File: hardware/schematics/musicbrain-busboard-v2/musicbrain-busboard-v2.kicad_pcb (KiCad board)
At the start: 2 copper layers, 200 x 115 mm, 94 parts, among them J1 SLOT 1, J10 EXP, J11 DISPLAY, J12 QWIIC, J13 MIDI IN1, J14 MIDI IN2, J15 MIDI OUT, J16 CAN, J17 AUDIO/CODEC, J18 TUNE, J19 DLG1, J2 SLOT 2, J20 DLG2, J21 EXPANSION, J3 SLOT 3, J4 SLOT 4, J5 SLOT 5, J6 SLOT 6, J7 HUB 1, J8 HUB 2, J9 PWR IN, U1 Teensy 4.1, U10 H11L1, U11 74LVC1G17, U12 SN65HVD230, U13 74LVC1G17, U2 R-78E5.0-0.5, U3 AMS1117-3.3, U4 74HC154, U5 74HC165, U6 74HC165, U7 74LVC1G125, U8 74LVC245, U9 H11L1

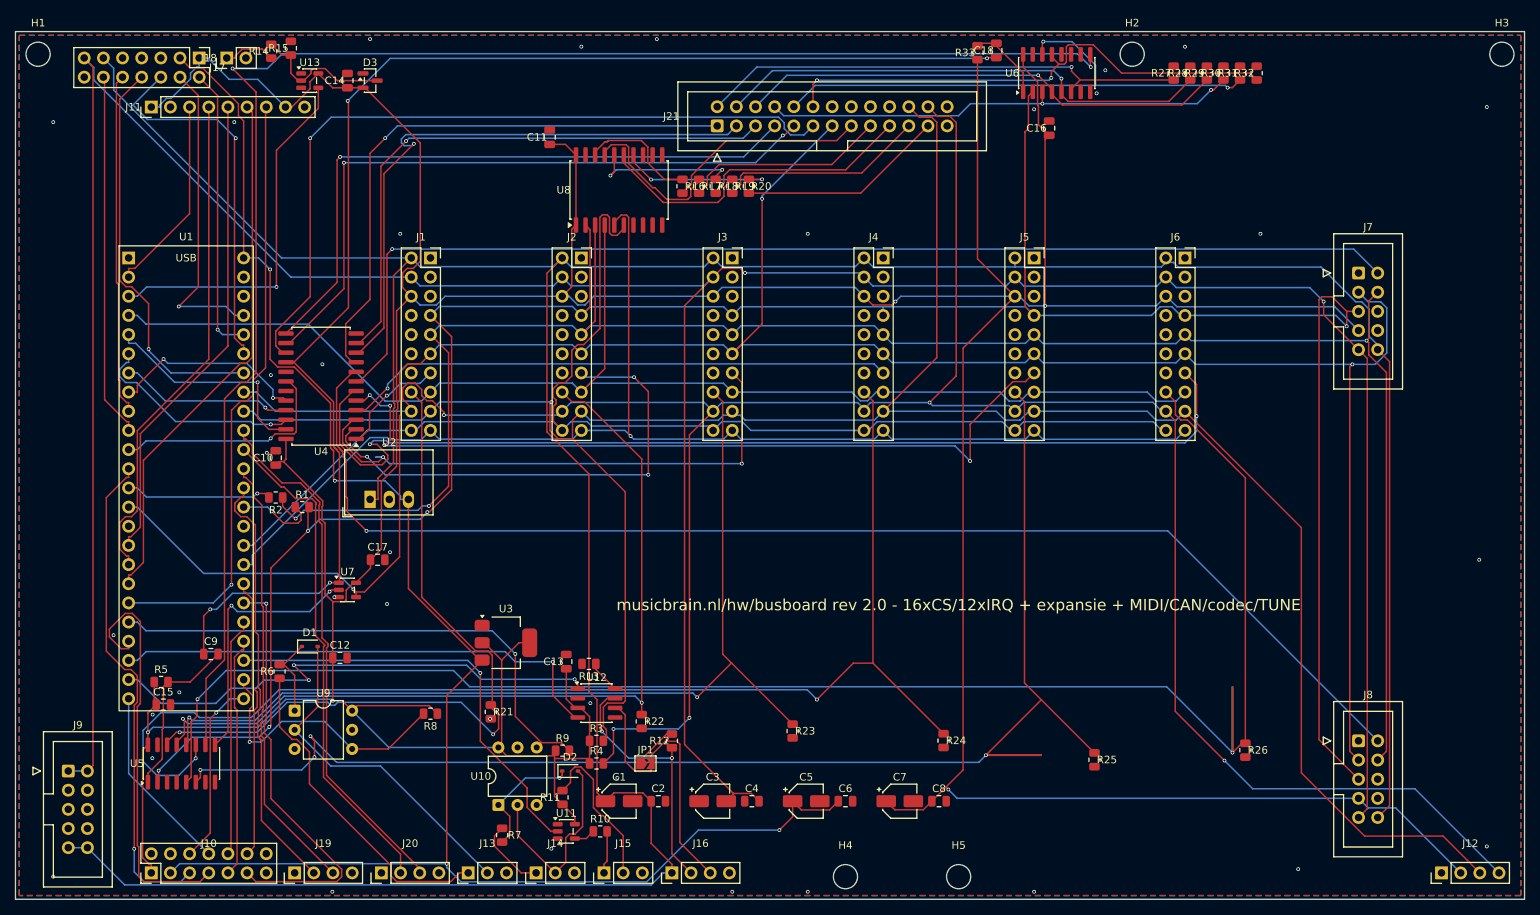
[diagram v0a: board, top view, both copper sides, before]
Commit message: busboard-v2: connector-labels verschoven (uit onder de headers)
Reference-labels van J7-J11/J17/J18/J21 handmatig verplaatst zodat ze niet meer
onder de connector-body vallen. KiCad heeft bij het opslaan het hele bestand
naar z'n native format herschreven (vandaar de grote diff); koper/connectiviteit
ongewijzigd - DRC 0 violations / 0 unconnected geverifieerd. Labelposities zijn
in gen_bus2_pcb.py REF_AT gesynct zodat een regeneratie ze behoudt.

Co-Authored-By: Claude Opus 4.8 <noreply@anthropic.com>
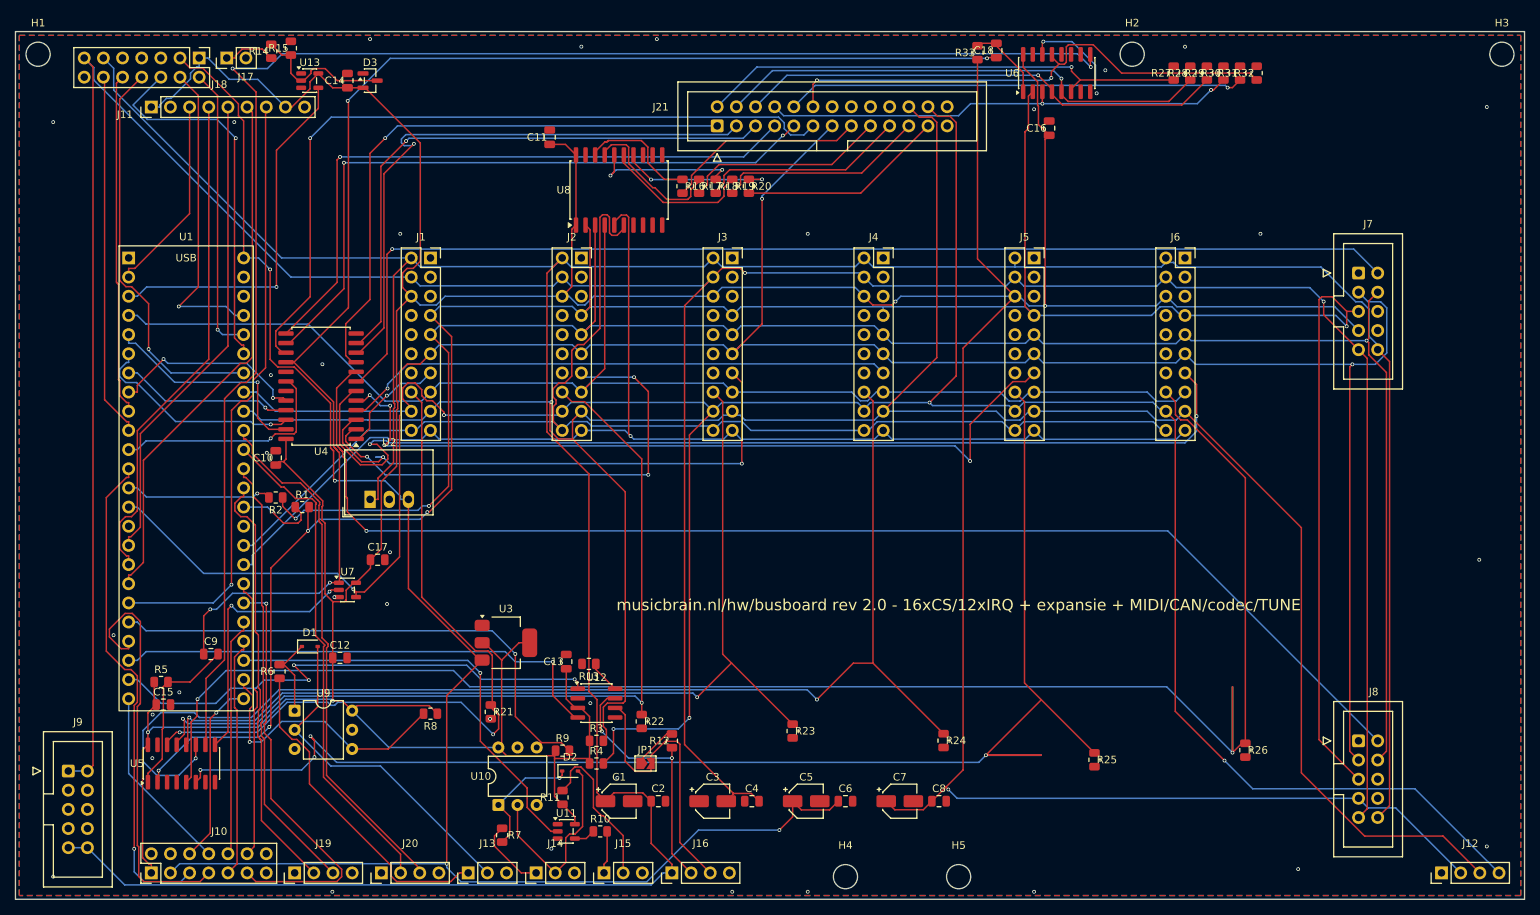
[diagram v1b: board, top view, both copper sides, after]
